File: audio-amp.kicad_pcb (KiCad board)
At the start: 2 copper layers, 60 x 38 mm, 48 parts, among them J1 AUDIO IN, J2 LEFT, J3 RIGHT, J4 24VDC, U1 TPA313xD2

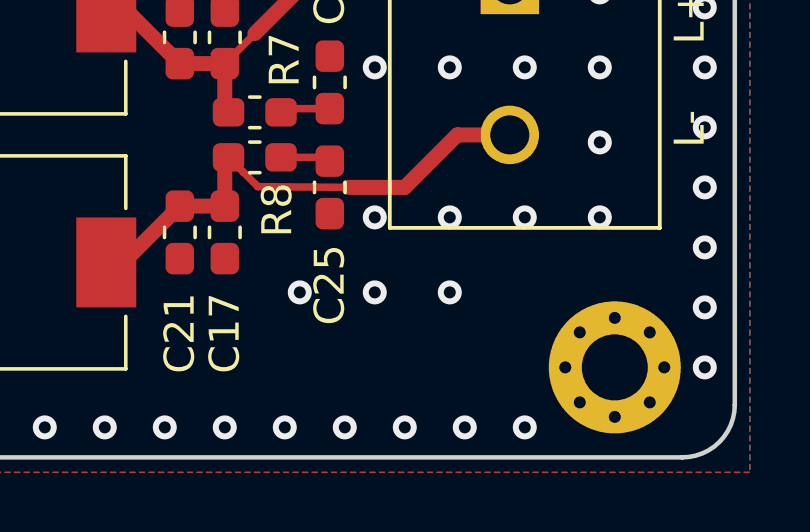
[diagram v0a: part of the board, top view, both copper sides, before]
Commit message: Add OSHW logo
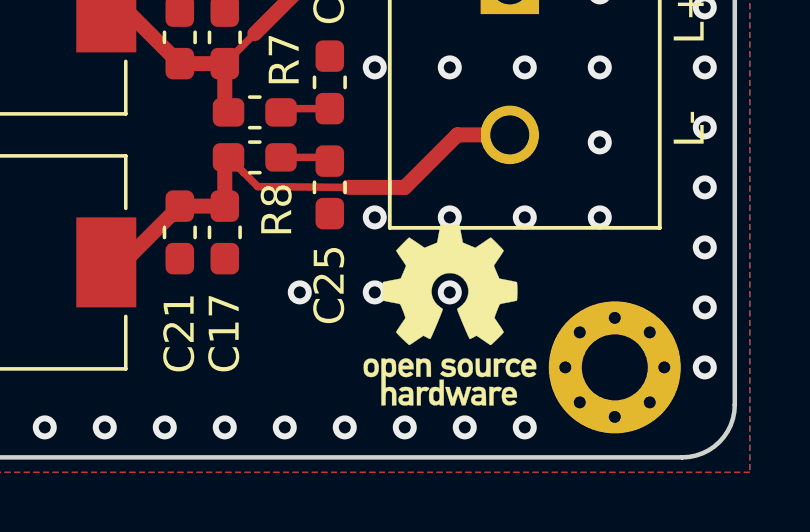
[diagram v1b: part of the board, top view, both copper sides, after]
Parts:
- added REF**: OSHW-Logo_5.7x6mm_SilkScreen, Symbol:OSHW-Logo_5.7x6mm_SilkScreen, F.Cu at (157.5, 163.2)

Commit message: progress on v2.
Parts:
- removed C20, C21, C22, C23: 1n, Capacitor_SMD:C_0603_1608Metric_Pad1.05x0.95mm_HandSolder
- removed C24, C25, C26, C27: 10n, Capacitor_SMD:C_0603_1608Metric_Pad1.05x0.95mm_HandSolder
- removed the J3 at (159.5, 142.8)
- removed R10, R7, R8, R9: 3.3, Resistor_SMD:R_0603_1608Metric_Pad1.05x0.95mm_HandSolder
- removed REF**: OSHW-Logo_5.7x6mm_SilkScreen, Symbol:OSHW-Logo_5.7x6mm_SilkScreen
- added C2: 10u, Capacitor_SMD:C_0805_2012Metric_Pad1.15x1.40mm_HandSolder, F.Cu at (121.5, 149.2)
- added JP1: Jumper_2_Open, Jumper:SolderJumper-2_P1.3mm_Open_RoundedPad1.0x1.5mm, F.Cu at (122.5, 156.0)
- added JP2: Jumper_2_Open, Jumper:SolderJumper-2_P1.3mm_Open_RoundedPad1.0x1.5mm, F.Cu at (122.5, 153.5)
- added R6: 39k, Resistor_SMD:R_0603_1608Metric_Pad1.05x0.95mm_HandSolder, F.Cu at (123.8, 136.2)
- added TP1: TestPoint, TestPoint:TestPoint_THTPad_D2.0mm_Drill1.0mm, F.Cu at (111.5, 151.5)
- added TP2: TestPoint, TestPoint:TestPoint_THTPad_D2.0mm_Drill1.0mm, F.Cu at (108.8, 138.8)
- added TP3: TestPoint, TestPoint:TestPoint_THTPad_D2.0mm_Drill1.0mm, F.Cu at (117.8, 135.2)
- added TP4: TestPoint, TestPoint:TestPoint_THTPad_D2.0mm_Drill1.0mm, F.Cu at (120.8, 135.2)
- added TP5: TestPoint, TestPoint:TestPoint_THTPad_D2.0mm_Drill1.0mm, F.Cu at (118.0, 151.5)
- added TP6: TestPoint, TestPoint:TestPoint_THTPad_D2.0mm_Drill1.0mm, F.Cu at (145.8, 155.5)
- added TP7: TestPoint, TestPoint:TestPoint_THTPad_D2.0mm_Drill1.0mm, F.Cu at (145.8, 159.5)
- added TP8: TestPoint, TestPoint:TestPoint_THTPad_D2.0mm_Drill1.0mm, F.Cu at (145.8, 138.5)
- added TP9: TestPoint, TestPoint:TestPoint_THTPad_D2.0mm_Drill1.0mm, F.Cu at (145.8, 142.5)
- C14: renamed from C16; value 680n -> 1u
- C15: renamed from C17; value 680n -> 1u
- C16: renamed from C18; value 680n -> 1u
- C17: renamed from C19; value 680n -> 1u
- J1: value AUDIO IN -> PJ-327ST-SMT
- J2: renamed from J4; value 24VDC -> DC-005C-25A
- J3: renamed from J2; value LEFT -> WJ126-5.0
- moved H1 24.0 mm to (111.0, 133.0)
- moved H3 23.8 mm to (111.2, 165.0)
- moved C15 9.65 mm to (145.0, 152.2), turned to 270 degrees
- moved C14 9.42 mm to (145.0, 162.8), turned to 270 degrees
- moved L1 9.33 mm to (139.5, 161.8)
- moved L2 8.87 mm to (139.5, 153.2)
- moved J3 6.50 mm to (153.0, 155.0)
- moved C1 4.56 mm to (111.2, 138.8), turned to 270 degrees
- moved C17 4.16 mm to (145.0, 145.8)
- moved C16 3.91 mm to (145.0, 135.2)
- moved L3 3.26 mm to (139.5, 136.2)
- moved L4 3.26 mm to (139.5, 144.8)
- moved C4 3.00 mm to (121.5, 151.2)
- moved C3 2.59 mm to (113.2, 138.8), turned to 270 degrees
- moved C5 2.02 mm to (123.2, 146.5)
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- renumbered C5 to C1, C15 to C10, C4 to C11, C6 to C12, C8 to C13, C9 to C18, C10 to C19, C2 to C3, C7 to C4, C11 to C5, C3 to C6, C12 to C7, C13 to C8, C14 to C9
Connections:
- C3 pad 1: GND -> Net-(C3-Pad1)
- C3 pad 2: Net-(C2-Pad2) -> GND
- J1 pad S: Net-(C2-Pad2) -> Net-(J1-PadS)
- U1 pad 12: Net-(U1-Pad12) -> +24V
- U1 pad 32: GND -> Net-(C3-Pad1)
- U1 pad 5: GND -> IP_L
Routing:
- net Net-(C3-Pad1): track 0.00 -> 18.1 mm
- net Net-(C17-Pad2): track 23.4 -> 7.60 mm
- net Net-(C16-Pad1): track 21.6 -> 7.72 mm
- net Net-(C14-Pad1): track 23.4 -> 9.80 mm
- net Net-(C15-Pad2): track 22.5 -> 9.80 mm, vias 0 -> 1
- net Net-(J1-PadS): track 0.00 -> 11.0 mm
- net Net-(C8-Pad1): track 17.7 -> 6.95 mm, vias 2 -> 0
- net Net-(C2-Pad2): track 10.4 -> 0.00 mm
- net IP_L: track 0.00 -> 9.18 mm
- net IN_R: track 14.1 -> 21.3 mm
- net +24V: track 72.4 -> 77.7 mm
- net Net-(C7-Pad1): track 10.7 -> 15.0 mm
- net Net-(C10-Pad1): track 10.8 -> 6.95 mm
- net IN_L: track 6.86 -> 10.2 mm
- net GND: track 20.4 -> 17.2 mm, vias 262 -> 191
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
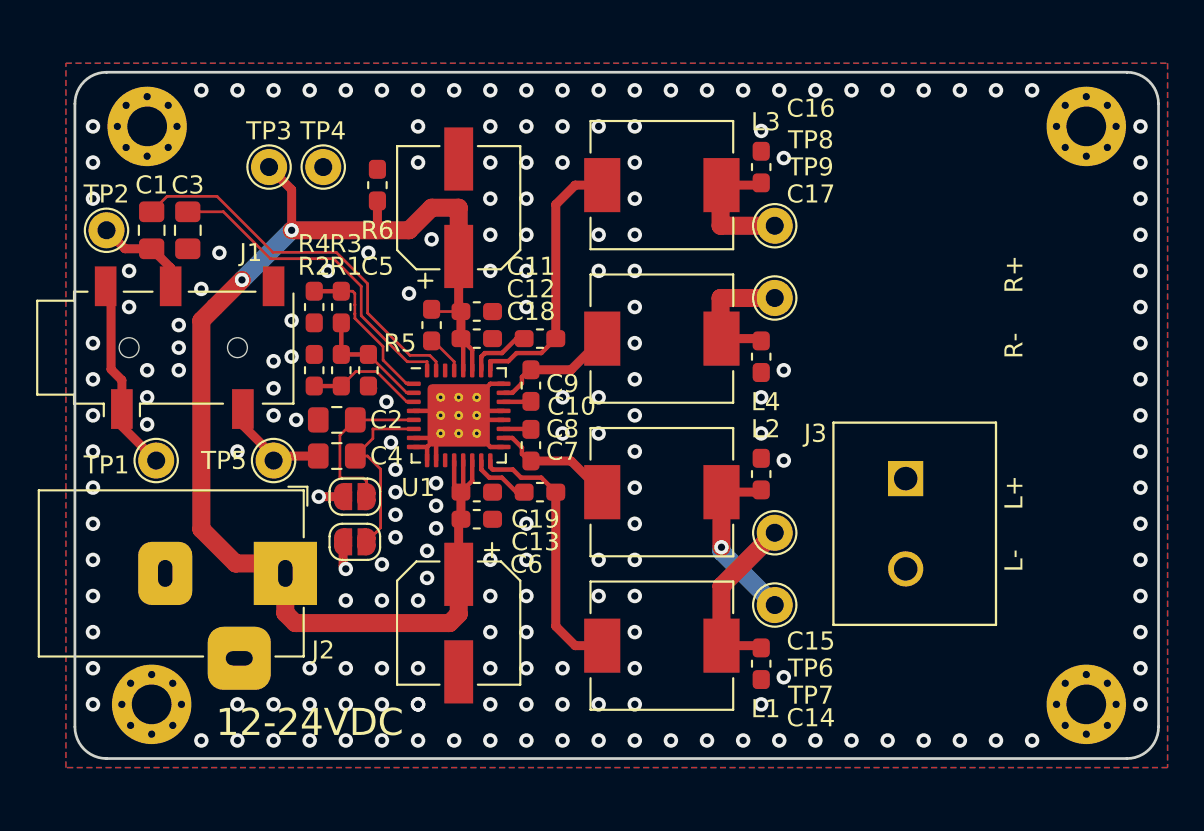
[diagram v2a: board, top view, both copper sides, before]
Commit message: Rev 2 done (probably)
This revision has

1. Correct capacitor filtering, with well-matched differential traces
2. The fault pin is no longer floating
3. The fault pin is now tied to the enable pin, allowing for
auto-restarting every 2 seconds.
4. The PVCC pin is now connected to power, instead of being left
disconnected like in the reference design.
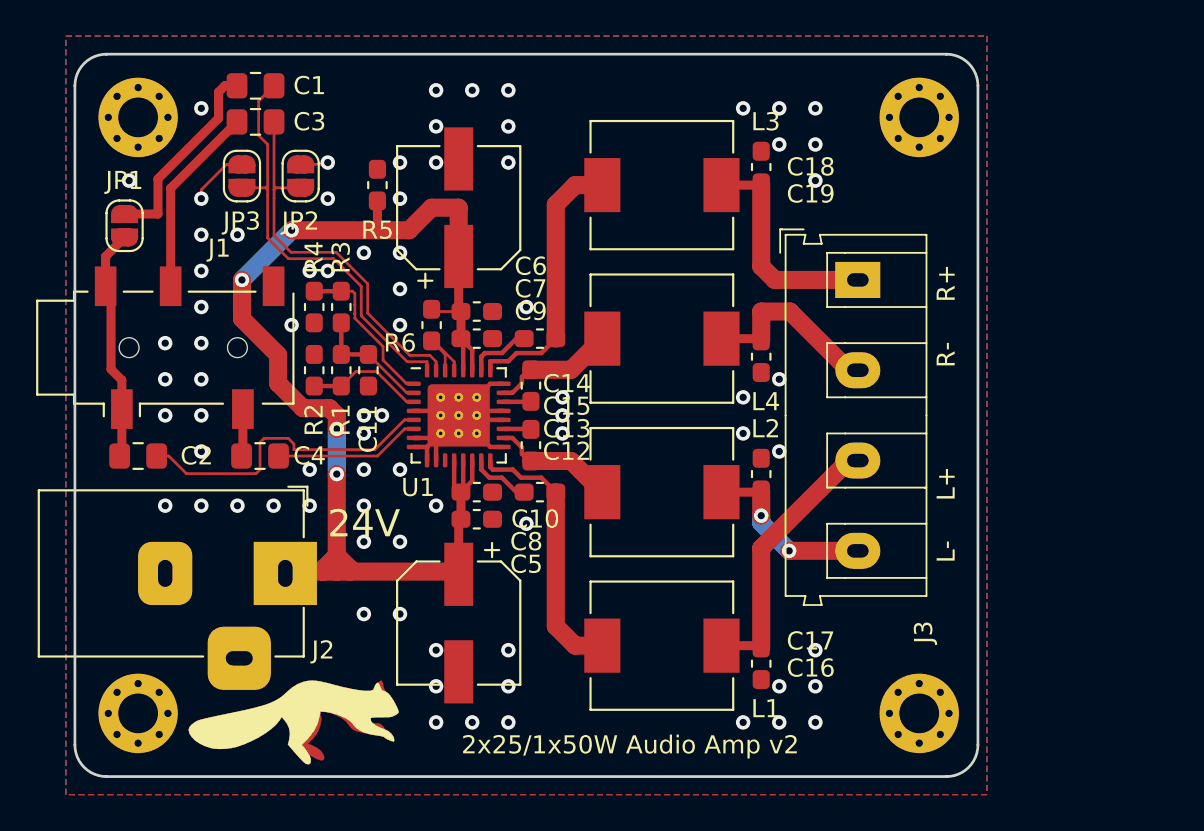
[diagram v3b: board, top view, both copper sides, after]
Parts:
- removed the C3 at (113.2, 138.8)
- removed TP1, TP2, TP3, TP4, TP5, TP6, TP7, TP8, TP9: TestPoint, TestPoint:TestPoint_THTPad_D2.0mm_Drill1.0mm
- added C2: 10u, Capacitor_SMD:C_0805_2012Metric_Pad1.15x1.40mm_HandSolder, F.Cu at (110.5, 151.2)
- added JP1: Jumper_2_Bridged, Jumper:SolderJumper-2_P1.3mm_Open_RoundedPad1.0x1.5mm, F.Cu at (109.8, 138.5)
- added Ref**: Val**, Squirrelly-McSquirrelface:squirrel-pcb, F.Cu at (119.3, 166.0)
- C11: renamed from C5; value 1u -> .1u
- J3: footprint OSTTA020161:OST_OSTTA020161 -> audio-amp:DG301_G-1x04_P5.0mm_Horizontal
- moved JP2 20.5 mm to (119.5, 135.8), turned to 90 degrees
- moved C1 19.0 mm to (117.0, 130.8)
- moved JP3 18.8 mm to (116.2, 135.8), turned to 90 degrees
- moved H3 9.26 mm to (153.8, 165.5)
- moved H4 9.26 mm to (153.8, 132.5)
- moved C3 8.31 mm to (117.0, 132.8), turned to 180 degrees
- moved J3 6.60 mm to (150.2, 149.0)
- moved C4 4.25 mm to (117.2, 151.2)
- moved H1 0.90 mm to (110.5, 165.5)
- moved H2 0.71 mm to (110.5, 132.5)
- renumbered C2 to C1, C19 to C10, C7 to C12, C8 to C13, C9 to C14, C10 to C15, C14 to C16, C15 to C17, C16 to C18, C17 to C19, C1 to C3, C6 to C5, C11 to C6, C12 to C7, C13 to C8, C18 to C9, H3 to H1, H1 to H2, H2 to H3, JP1 to JP2, JP2 to JP3, R6 to R5, R5 to R6
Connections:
- C1 pad 1: IP_L -> INNR
- C1 pad 2: GND -> Net-(C1-Pad2)
- C16 pad 1: Net-(C14-Pad1) (its old number) -> Net-(C16-Pad1)
- C17 pad 2: Net-(C15-Pad2) (its old number) -> Net-(C17-Pad2)
- C18 pad 1: Net-(C16-Pad1) -> Net-(C18-Pad1)
- C19 pad 2: Net-(C17-Pad2) -> Net-(C19-Pad2)
- C3 pad 1: IN_R -> INPR
- C4 pad 1: IN_L -> INPL
- H2 pad 1: GND -> Net-(H2-Pad1)
- H3 pad 1: GND -> Net-(H3-Pad1)
- H4 pad 1: GND -> Net-(H4-Pad1)
- J3 pad 1: Net-(C14-Pad1) (its old number) -> Net-(C18-Pad1)
- J3 pad 2: Net-(C15-Pad2) (its old number) -> Net-(C19-Pad2)
- JP2 pad 1: IN_L -> INPR
- JP3 pad 1: IP_L -> INNR
- L1 pad 1: Net-(C14-Pad1) (its old number) -> Net-(C16-Pad1)
- L2 pad 1: Net-(C15-Pad2) (its old number) -> Net-(C17-Pad2)
- L3 pad 1: Net-(C16-Pad1) -> Net-(C18-Pad1)
- L4 pad 1: Net-(C17-Pad2) -> Net-(C19-Pad2)
- R6 pad 1: Net-(R5-Pad1) -> Net-(R6-Pad1)
- U1 pad 29: Net-(R5-Pad1) -> Net-(R6-Pad1)
- U1 pad 30: Net-(U1-Pad30) -> Net-(R6-Pad1)
- U1 pad 31: IN_R -> INPR
- U1 pad 32: Net-(C3-Pad1) -> INNR
- U1 pad 5: IP_L -> INNL
- U1 pad 6: IN_L -> INPL
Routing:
- net INNR: track 0.00 -> 23.5 mm
- net IN_R: track 21.3 -> 0.00 mm
- net INPR: track 0.00 -> 21.1 mm
- net Net-(C3-Pad1): track 18.1 -> 0.00 mm
- net INNL: track 0.00 -> 17.5 mm
- net Net-(C18-Pad1): track 0.00 -> 12.6 mm
- net Net-(C1-Pad2): track 0.00 -> 11.2 mm
- net Net-(C19-Pad2): track 0.00 -> 10.5 mm
- net IN_L: track 10.2 -> 0.00 mm
- net Net-(C15-Pad2) (its old number): track 9.80 -> 0.00 mm, vias 1 -> 0
- net Net-(C14-Pad1) (its old number): track 9.80 -> 0.00 mm
- net IP_L: track 9.18 -> 0.00 mm
- net INPL: track 0.00 -> 8.11 mm
- net +24V: track 77.7 -> 69.9 mm, vias 2 -> 4
- net Net-(C16-Pad1): track 7.72 -> 15.3 mm
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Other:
- board size 60 x 38 mm -> 50 x 40 mm
- board text added: "24V"
- board text added: "2x25/1x50W Audio Amp v2"
- board text removed: "12-24VDC"
